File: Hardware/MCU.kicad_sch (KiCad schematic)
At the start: 33 parts, among them SW1 reset, SW2 MCU_BOOT, U7 STM32H743VITx, Y1 ASE-8.000MHZ-LC-T

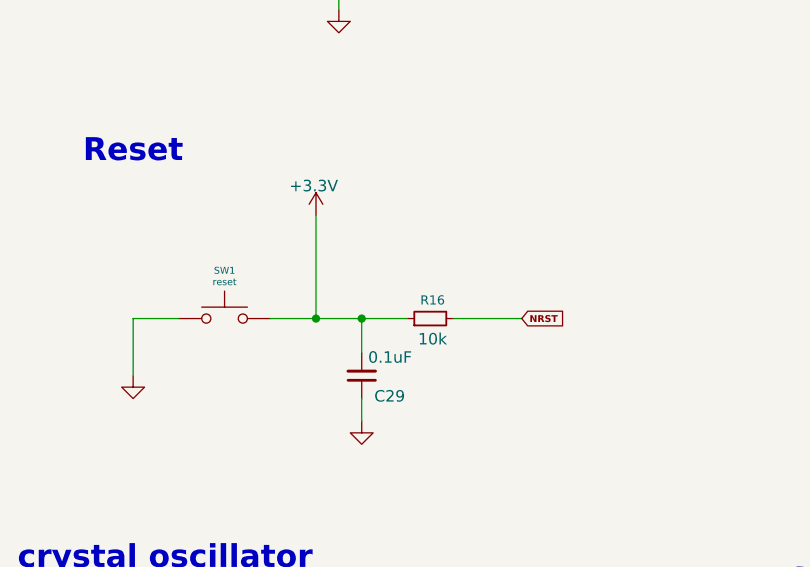
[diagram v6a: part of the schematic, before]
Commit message: fixed the reset schematics
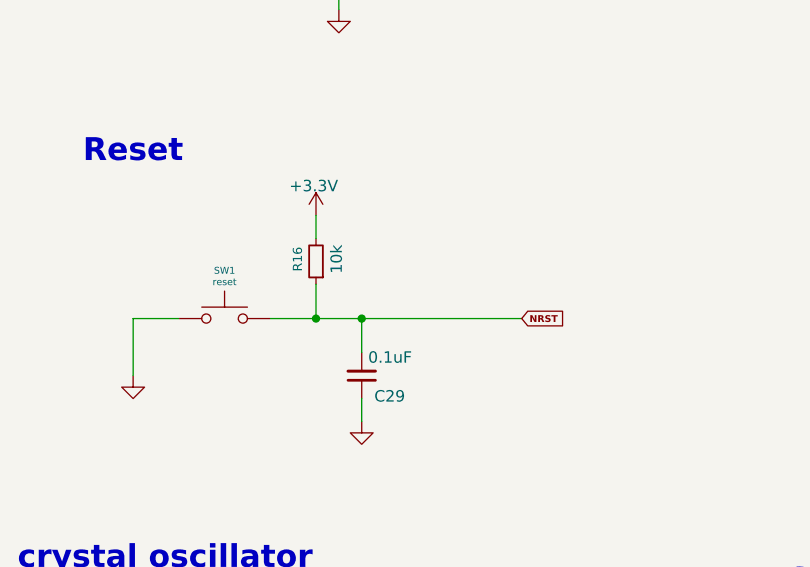
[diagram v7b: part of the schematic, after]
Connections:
- net +3.3V: now also R16.2; no longer C29.2, R16.1, SW1.2
- net NRST: now also C29.2, R16.1, SW1.2; no longer R16.2
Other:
- moved on the sheet: R16
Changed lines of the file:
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@@
 	(wire
 		(pts
+			(xy 68.58 186.69) (xy 68.58 190.5)
+		)
+		(stroke
+			(width 0)
+			(type default)
+		)
+	)
+	(wire
+		(pts
 			(xy 73.66 201.93) (xy 73.66 199.39)
 		)
@@
 	(wire
 		(pts
-			(xy 83.82 190.5) (xy 91.44 190.5)
-		)
-		(stroke
-			(width 0)
-			(type default)
-		)
-	)
-	(wire
-		(pts
 			(xy 57.15 226.06) (xy 57.15 228.6)
 		)
@@
 	(wire
 		(pts
-			(xy 78.74 190.5) (xy 73.66 190.5)
+			(xy 73.66 190.5) (xy 91.44 190.5)
 		)
 		(stroke
@@
 	(wire
 		(pts
-			(xy 68.58 179.07) (xy 68.58 190.5)
+			(xy 68.58 179.07) (xy 68.58 181.61)
 		)
 		(stroke
@@
 	(symbol
 		(lib_id "Device:R_Small")
-		(at 81.28 190.5 90)
+		(at 68.58 184.15 180)
 		(unit 1)
 		(exclude_from_sim no)
@@
 		(dnp no)
 		(property "Reference" "R16"
-			(at 81.534 188.468 90)
+			(at 66.548 183.896 90)
 			(effects
 				(font
@@
 		)
 		(property "Value" "10k"
-			(at 81.534 192.786 90)
+			(at 70.866 183.896 90)
 			(effects
 				(font
@@
 		)
 		(property "Footprint" "Resistor_SMD:R_0402_1005Metric"
-			(at 81.28 190.5 0)
+			(at 68.58 184.15 0)
 			(effects
 				(font
@@
 		)
 		(property "Datasheet" "~"
-			(at 81.28 190.5 0)
+			(at 68.58 184.15 0)
 			(effects
 				(font
@@
 		)
 		(property "Description" "Resistor, small symbol"
-			(at 81.28 190.5 0)
+			(at 68.58 184.15 0)
 			(effects
 				(font
@@
 		)
 		(property "Link" ""
-			(at 81.28 190.5 90)
+			(at 68.58 184.15 90)
 			(effects
 				(font

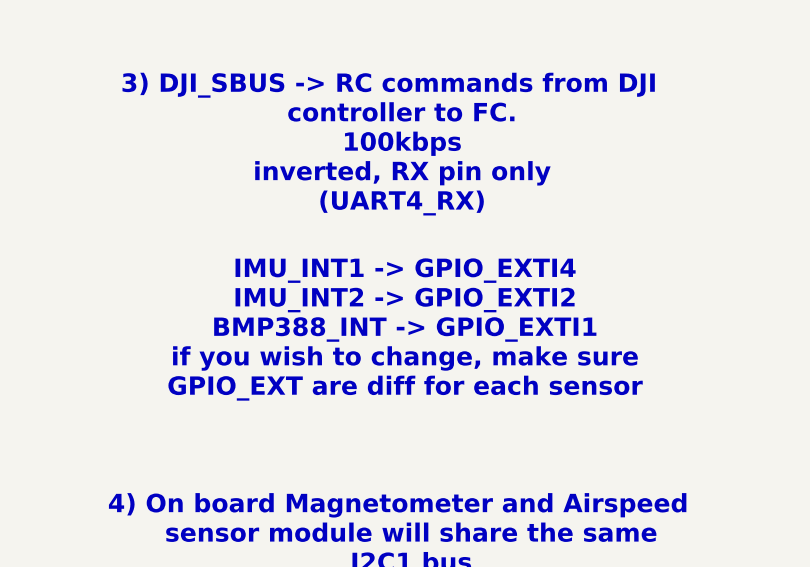
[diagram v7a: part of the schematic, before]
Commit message: added quatronion filter, CRSF protocol, and PID loops
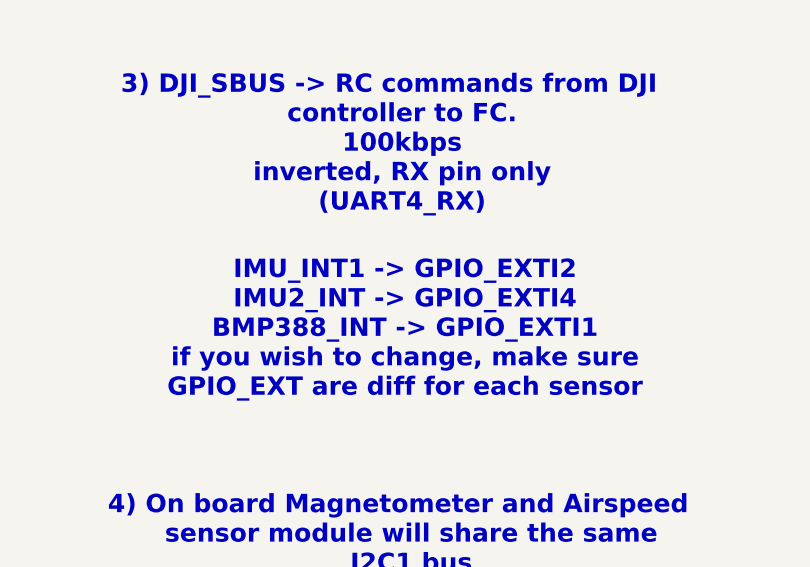
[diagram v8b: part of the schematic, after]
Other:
- note added: "IMU_INT1 -> GPIO_EXTI2 IMU2_INT -> GPIO_EXTI4 BMP388_INT -> GPIO_EXTI1 if you wish to change, make sure GPIO_EXT are diff for each sensor"
- note removed: "IMU_INT1 -> GPIO_EXTI4 IMU_INT2 -> GPIO_EXTI2 BMP388_INT -> GPIO_EXTI1 if you wish to change, make sure GPIO_EXT are diff for each sensor"
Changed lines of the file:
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@@
 		)
 	)
-	(text "IMU_INT1 -> GPIO_EXTI4\nIMU_INT2 -> GPIO_EXTI2\nBMP388_INT -> GPIO_EXTI1\nif you wish to change, make sure  \nGPIO_EXT are diff for each sensor"
+	(text "IMU_INT1 -> GPIO_EXTI2\nIMU2_INT -> GPIO_EXTI4\nBMP388_INT -> GPIO_EXTI1\nif you wish to change, make sure  \nGPIO_EXT are diff for each sensor"
 		(exclude_from_sim no)
 		(at 380.746 119.38 0)
